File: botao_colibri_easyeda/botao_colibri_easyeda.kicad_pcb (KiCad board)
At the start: 2 copper layers, 79 x 137.8 mm, 19 parts, among them J1 HDR-M-2.54_1X1, J1 PJ-307C, U1 CONN-TH_10P-P2.00_PHD2.0MM-2X5, U1 HM-11, U1 MIC5365-3.3YC5-TR 3.3V REGULA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, U1 TP4056-protect

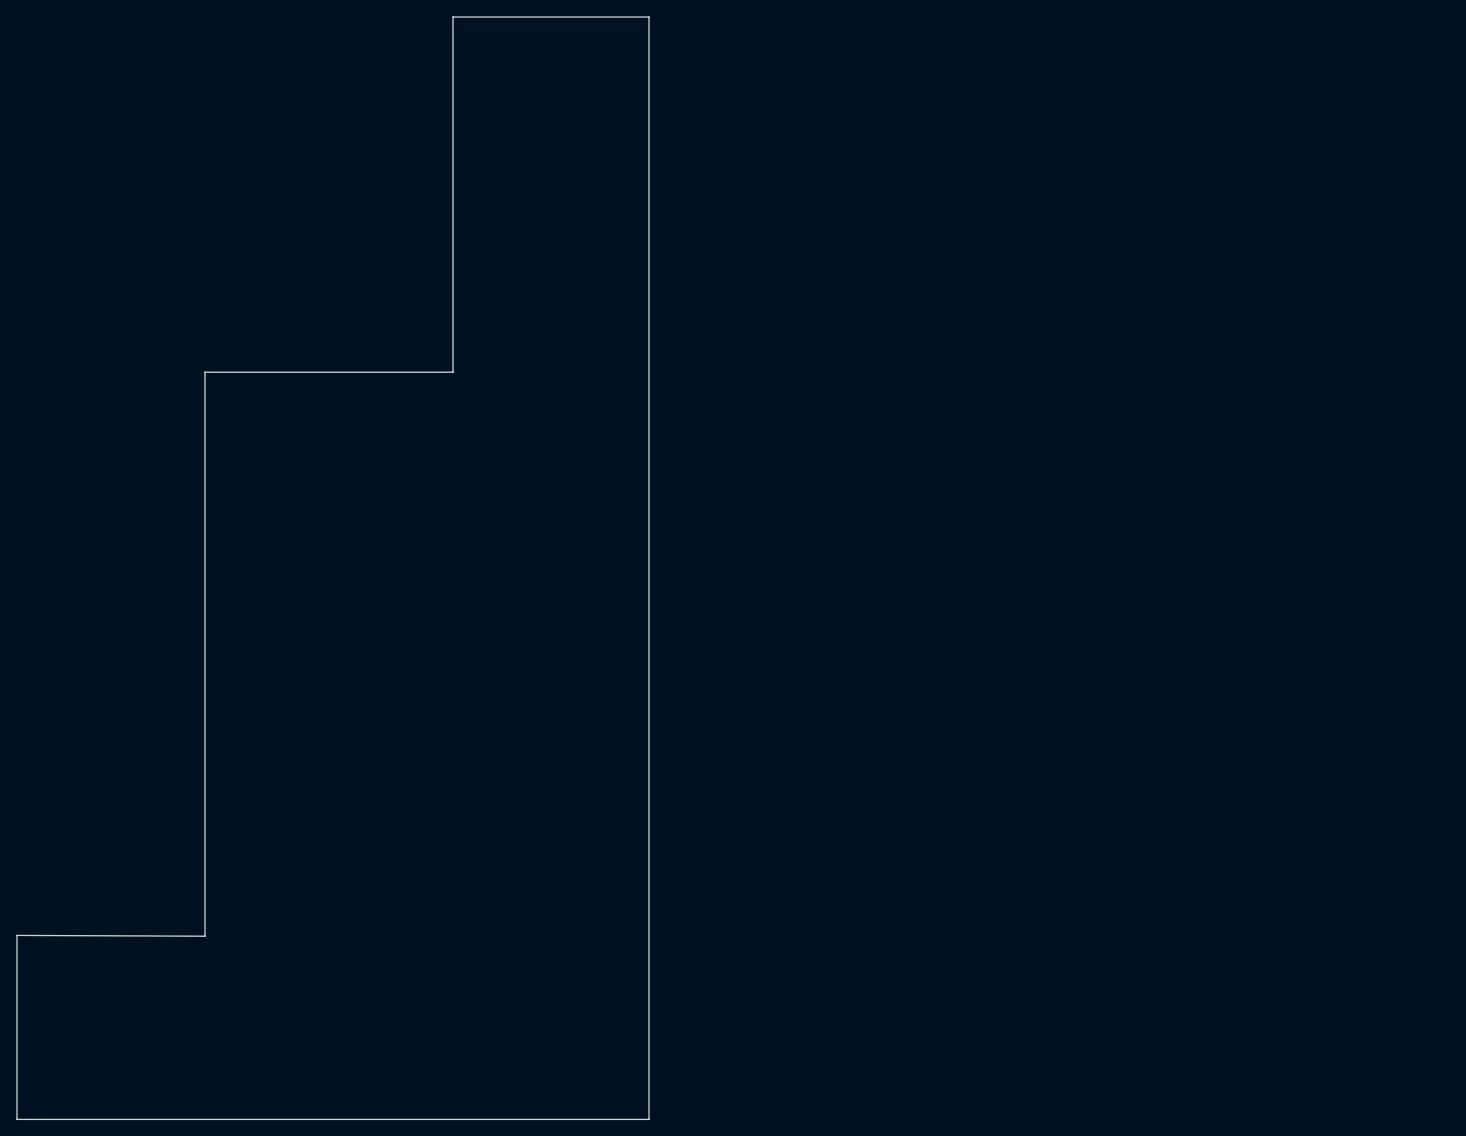
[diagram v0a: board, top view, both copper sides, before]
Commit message: fix: Reimport EasyEDA PCB with complete board data
- Use PCB_PCB_botao-bt-copy_2026-07-03.json as source
- Correct Edge.Cuts import (outer contour + internal cutout)
- Import copper tracks, vias and NPTH mechanical holes
- Update converted KiCad project board file
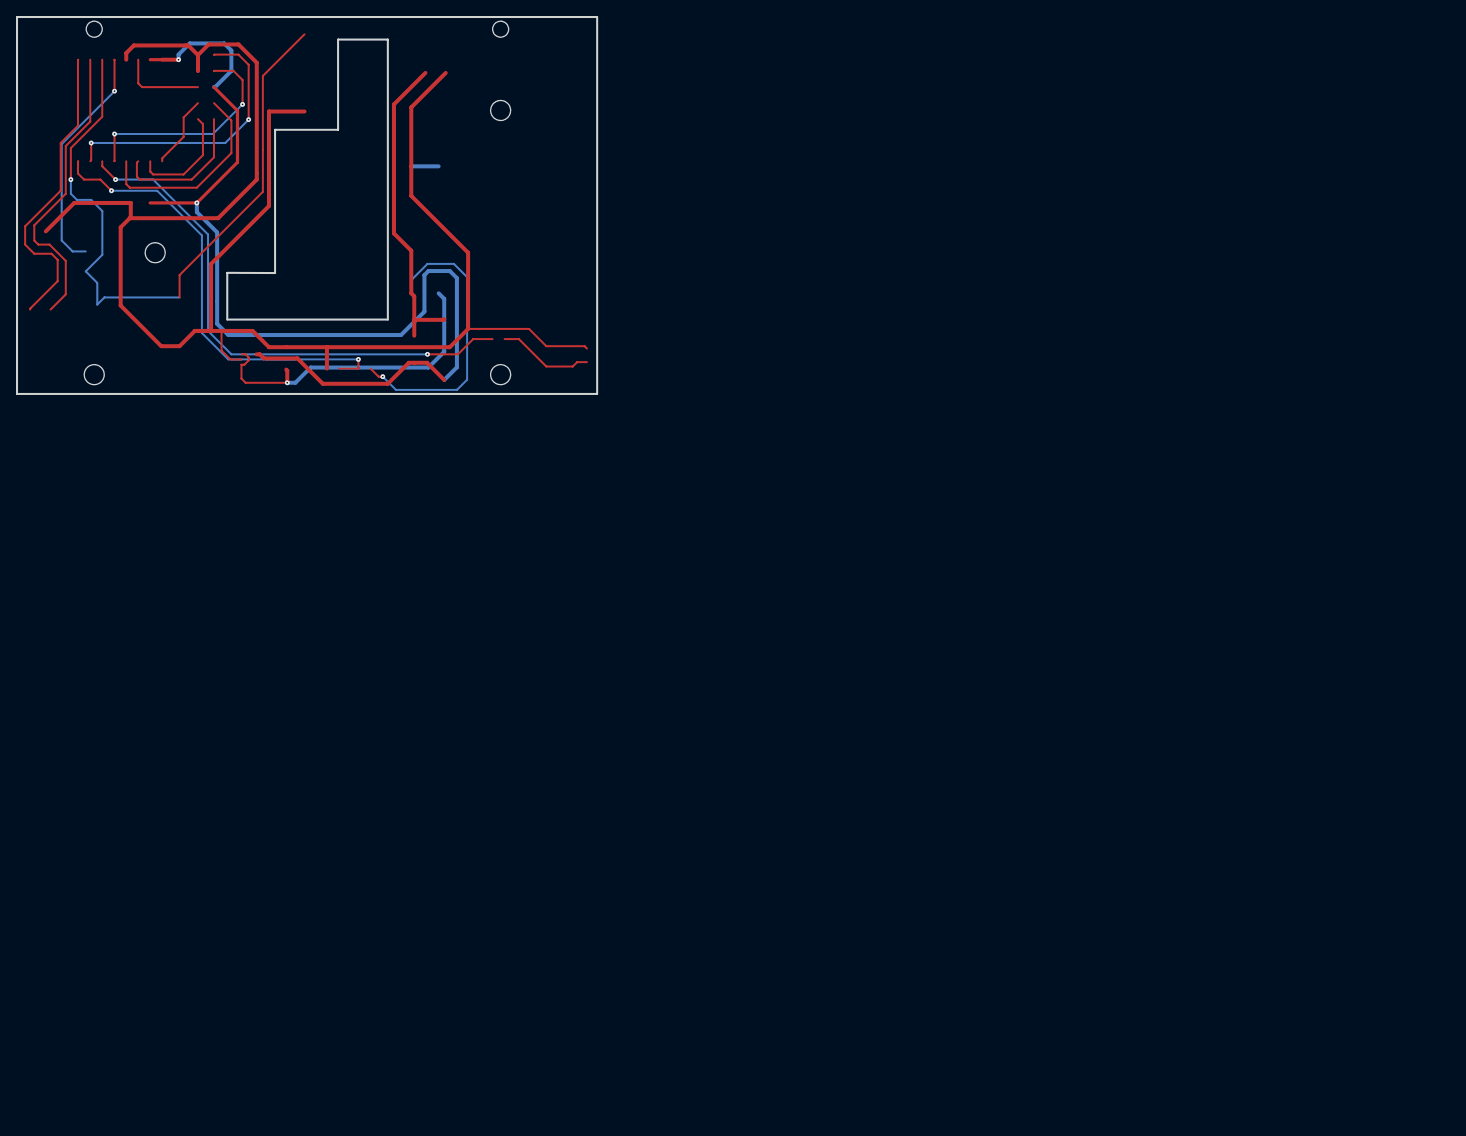
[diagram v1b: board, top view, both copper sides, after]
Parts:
- removed C1 (x2): C1206, C1206
- removed D1: 1N4007W, SOD-123_L2.8-W1.8-LS3.7-RD
- removed D1: 1N4007W, DIODE
- removed the H1 at (102.5, 16.4)
- removed the H1 at (-92.0, 132.9)
- removed J1 (x3): HDR-M-2.54_1X1, HDR-M-2.54_1X1
- removed J1: PJ-307C, AUDIO-TH_PJ307C
- removed L1: 19-217/R6C-AL1M2VY/3T, LED 5MM
- removed L1: 19-217/R6C-AL1M2VY/3T, LED0603_RED
- removed R1 (x3): R0603, R0603
- removed U1: CONN-TH_10P-P2.00_PHD2.0MM-2X5, CONN-TH_10P-P2.00_PHD2.0MM-2X5
- removed U1: TP4056-protect, TP4056
- removed U1: HM-11, HM-11
- removed U1: MIC5365-3.3YC5-TR 3.3V REGULATOR, MIC5365-3.3YC5-TR 3.3V REGULATOR
- added H1: NPTH, NPTH, F.Cu at (60.5, 11.7)
- added H2: NPTH, NPTH, F.Cu at (9.65, 44.7)
- added H3: NPTH, NPTH, F.Cu at (60.5, 44.7)
- added H4: NPTH, NPTH, F.Cu at (17.3, 29.5)
- added H5: NPTH, NPTH, F.Cu at (9.65, 1.52)
- added H6: NPTH, NPTH, F.Cu at (60.5, 1.52)
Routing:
- net 0: track 0.00 -> 947.7 mm, vias 0 -> 14
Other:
- board size 79 x 137.8 mm -> 72.5 x 47.1 mm
- board text added: "4.5 AUDIO-TH_PJ307C"
- board text added: "4.5 C1206"
- board text added: "4.5 CONN-TH_10P-P2.00_PHD2.0MM-2X5"
- board text added: "4.5 DIODE"
- board text added: "4.5 HDR-F-2.54_1X2"
- board text added: "4.5 HDR-M-2.54_1X1"
- board text added: "4.5 HM-11"
- board text added: "4.5 LED 5MM"
- board text added: "4.5 LED0603_RED"
- board text added: "4.5 MIC5365-3.3YC5-TR 3.3V REGULATOR"
- board text added: "4.5 R0603"
- board text added: "4.5 SOD-123_L2.8-W1.8-LS3.7-RD"
- board text added: "4.5 TP4056"
- board text added: "5.5118"

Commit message: LImpeza board placa botão
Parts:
- moved H1 121.7 mm to (167.0, 70.5)
- moved H2 121.7 mm to (116.2, 103.5)
- moved H3 121.7 mm to (167.0, 103.5)
- moved H4 121.7 mm to (123.8, 88.2)
- moved H5 121.7 mm to (116.2, 60.3)
- moved H6 121.7 mm to (167.0, 60.3)
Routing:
- net 0: track 947.7 -> 0.00 mm, vias 14 -> 0
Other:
- board text removed: "4.5 AUDIO-TH_PJ307C"
- board text removed: "4.5 C1206"
- board text removed: "4.5 CONN-TH_10P-P2.00_PHD2.0MM-2X5"
- board text removed: "4.5 DIODE"
- board text removed: "4.5 HDR-F-2.54_1X2"
- board text removed: "4.5 HDR-M-2.54_1X1"
- board text removed: "4.5 HM-11"
- board text removed: "4.5 LED 5MM"
- board text removed: "4.5 LED0603_RED"
- board text removed: "4.5 MIC5365-3.3YC5-TR 3.3V REGULATOR"
- board text removed: "4.5 R0603"
- board text removed: "4.5 SOD-123_L2.8-W1.8-LS3.7-RD"
- board text removed: "4.5 TP4056"
- board text removed: "5.5118"
